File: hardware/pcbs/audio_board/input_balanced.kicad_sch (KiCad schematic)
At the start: 25 parts, among them J1 NC3FAH1, U3 OPA1678

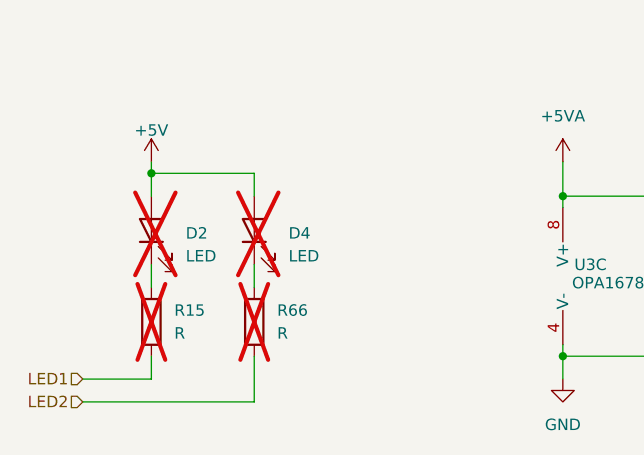
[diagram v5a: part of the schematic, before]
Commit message: pcbs: update purchase info
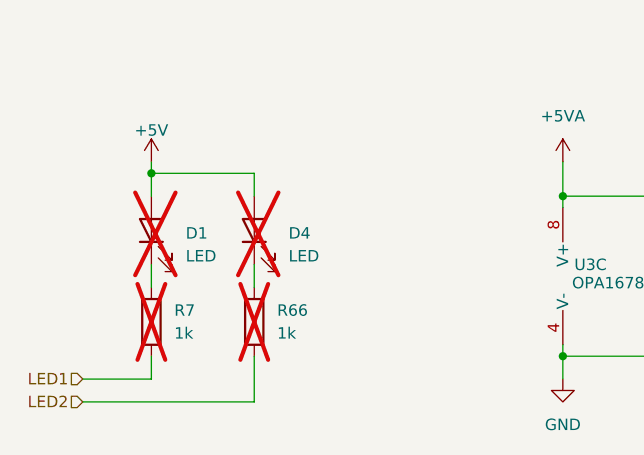
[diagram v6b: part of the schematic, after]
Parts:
- C12, C13, C18, C9: Part (none) -> C 10μF 16V 0805; Shop (none) -> https://store.comet.bg/Catalogue/Product/36934/
- C14: Part (none) -> C 33nF 16V 0603; Shop (none) -> https://store.comet.bg/Catalogue/Product/7009/
- C16, C17: Part (none) -> C 100nF 16V 0603; Shop (none) -> https://store.comet.bg/Catalogue/Product/38000/
- C5, C8: Part (none) -> C 100pF 16V 0603; Shop (none) -> https://store.comet.bg/Catalogue/Product/37094/
- D1: renamed from D2; Part (none) -> RED LED 0603; Shop (none) -> https://store.comet.bg/Catalogue/Product/48021/
- D4: Part (none) -> RED LED 0603; Shop (none) -> https://store.comet.bg/Catalogue/Product/48021/
- J1: Part (none) -> NC3FAH1; Shop (none) -> https://eu.mouser.com/ProductDetail/Neutrik/NC3FAH1?qs=jCym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
- R1, R3, R5: Part (none) -> R 10kΩ 125mW 1% 0603; Shop (none) -> https://store.comet.bg/Catalogue/Product/4415/
- R10, R16, R17, R2, R4, R9: Part (none) -> R 22kΩ 125mW 1% 0603; Shop (none) -> https://store.comet.bg/Catalogue/Product/4419/
- R66: value R -> 1k; Part (none) -> R 1kΩ 125mW 1% 0603; Shop (none) -> https://store.comet.bg/Catalogue/Product/3458/
- R7: renamed from R15; value R -> 1k; Part (none) -> R 1kΩ 125mW 1% 0603; Shop (none) -> https://store.comet.bg/Catalogue/Product/3458/
- R8: Part (none) -> R 220Ω 125mW 1% 0603; Shop (none) -> https://store.comet.bg/Catalogue/Product/4397/
- U3: value OPA1678 -> OPA1678; Part (none) -> OPA1678IDR; Shop (none) -> https://eu.mouser.com/ProductDetail/Texas-Instruments/OPA16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

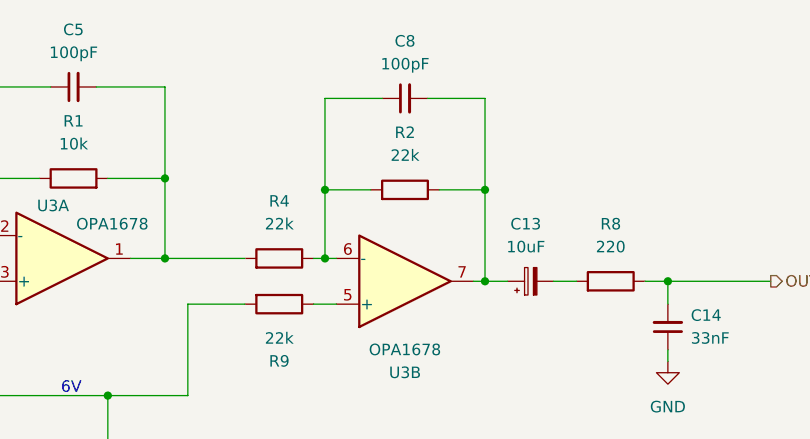
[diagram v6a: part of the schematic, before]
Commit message: audio_board: implement input level boost
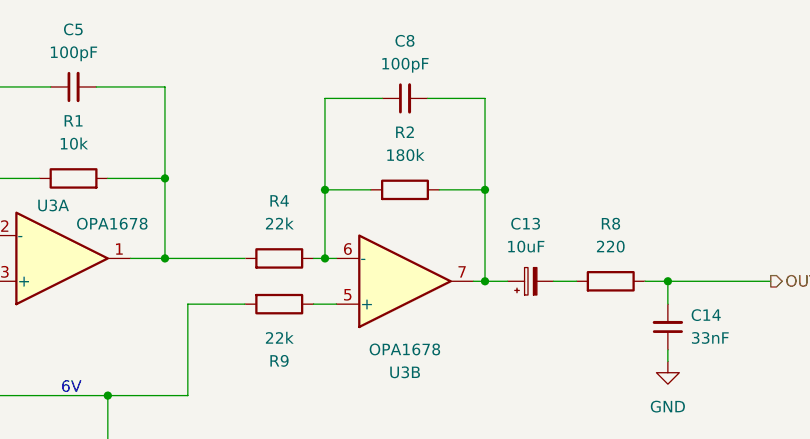
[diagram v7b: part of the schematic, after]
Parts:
- R2: value 22k -> 180k; LCSC C31850 -> (none); MPN 560112116022 -> (none); Part R 22kΩ 125mW 1% 0603 -> R 180kΩ 125mW 1% 0603; Shop https://store.comet.bg/Catalogue/Product/4419/ -> https://store.comet.bg/Catalogue/Product/4787/
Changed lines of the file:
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@@
 			)
 		)
-		(property "Value" "22k"
+		(property "Value" "180k"
 			(at 182.88 66.04 90)
 			(effects
@@
 			)
 		)
-		(property "LCSC" "C31850"
+		(property "LCSC" ""
 			(at 182.88 69.85 0)
 			(effects
@@
 			)
 		)
-		(property "MPN" "560112116022 "
+		(property "MPN" ""
 			(at 182.88 69.85 0)
 			(effects
@@
 			)
 		)
-		(property "Part" "R 22kΩ 125mW 1% 0603"
+		(property "Part" "R 180kΩ 125mW 1% 0603"
 			(at 182.88 69.85 0)
 			(effects
@@
 			)
 		)
-		(property "Shop" "https://store.comet.bg/Catalogue/Product/4419/"
+		(property "Shop" "https://store.comet.bg/Catalogue/Product/4787/"
 			(at 182.88 69.85 0)
 			(effects
